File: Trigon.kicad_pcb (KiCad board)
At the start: 2 copper layers, 160 x 120 mm, 50 parts, among them U1 ProMicro

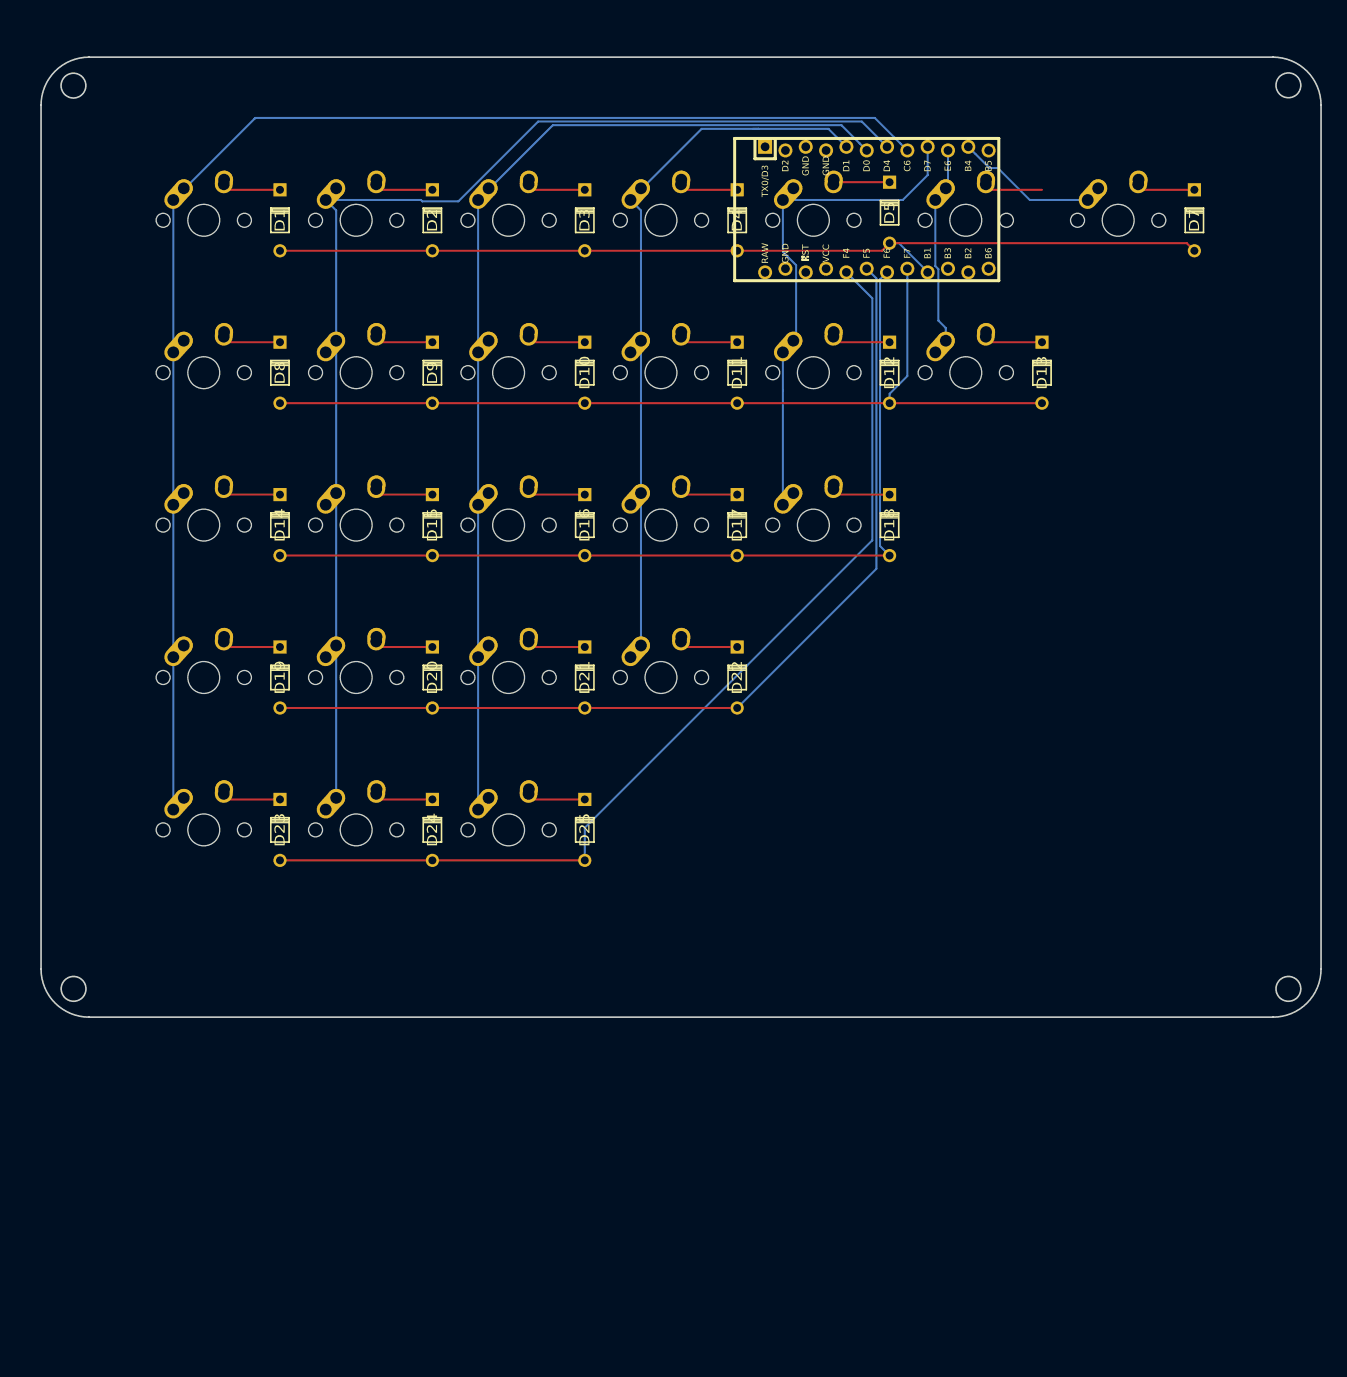
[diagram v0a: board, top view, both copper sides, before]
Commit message: routed without rows cols
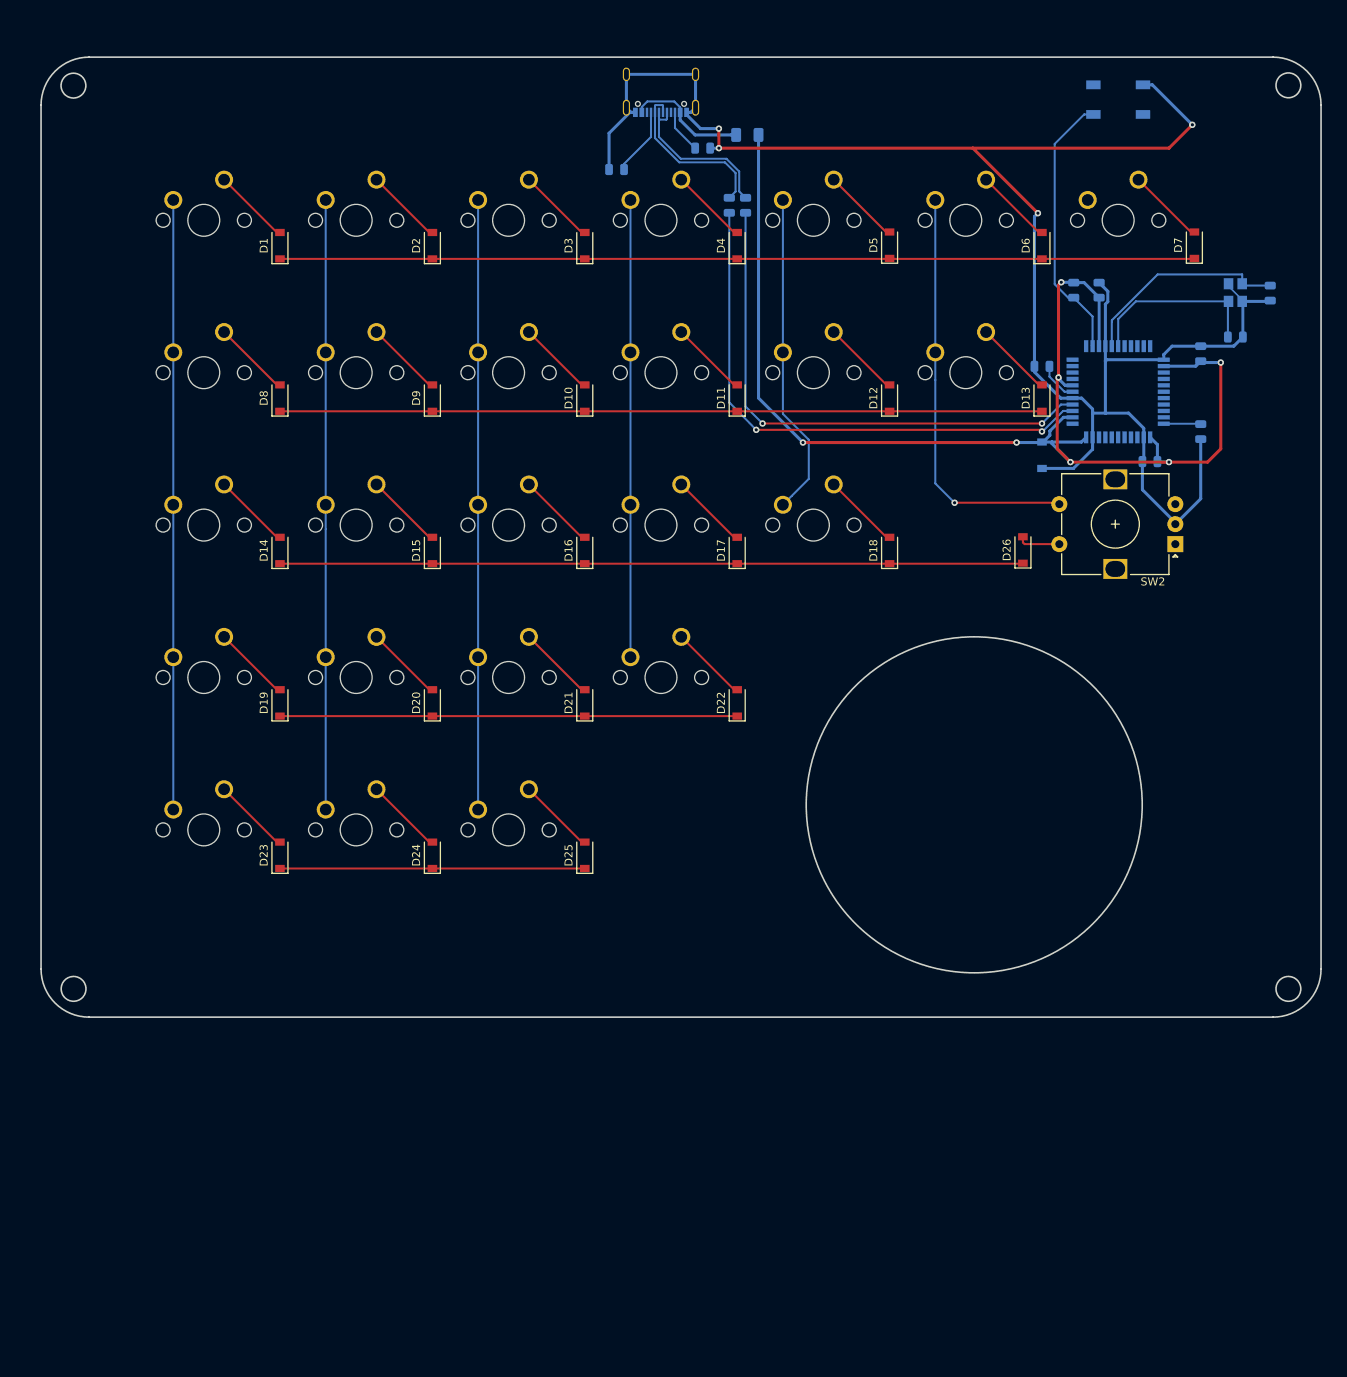
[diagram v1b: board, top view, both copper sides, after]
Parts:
- added C1: 22pF, Capacitor_SMD:C_0805_2012Metric, B.Cu at (148.0, -80.7)
- added C2: 22pF, Capacitor_SMD:C_0805_2012Metric, B.Cu at (152.4, -86.2)
- added C3: 1uF, Capacitor_SMD:C_0805_2012Metric, B.Cu at (123.8, -77.0)
- added C4: 0.1uF, Capacitor_SMD:C_0805_2012Metric, B.Cu at (143.7, -78.6)
- added C5: 0.1uF, Capacitor_SMD:C_0805_2012Metric, B.Cu at (137.3, -65.1)
- added C6: 0.1uF, Capacitor_SMD:C_0805_2012Metric, B.Cu at (131.0, -86.5)
- added C7: 10uF, Diode_SMD:D_SOD-123, B.Cu at (123.8, -65.9)
- added D26: D_Small, Diode_SMD:D_SOD-123, F.Cu at (121.4, -54.0)
- added D6: D_Small, Diode_SMD:D_SOD-123, F.Cu at (123.8, -92.1)
- added F1: Polyfuse_Small, Fuse:Fuse_1206_3216Metric, B.Cu at (87.0, -105.9)
- added J1: USB_C_Receptacle_USB2.0, Connector_USB:USB_C_Receptacle_Palconn_UTC16-G, B.Cu at (76.2, -111.3)
- added R1: 22, Resistor_SMD:R_0805_2012Metric, B.Cu at (86.8, -97.1)
- added R2: 22, Resistor_SMD:R_0805_2012Metric, B.Cu at (84.7, -97.1)
- added R3: 10k, Resistor_SMD:R_0805_2012Metric, B.Cu at (127.8, -86.5)
- added R4: R_Small, Resistor_SMD:R_0805_2012Metric, B.Cu at (70.6, -101.6)
- added R5: R_Small, Resistor_SMD:R_0805_2012Metric, B.Cu at (81.4, -104.3)
- added R6: 10k, Resistor_SMD:R_0805_2012Metric, B.Cu at (143.7, -68.8)
- added SW1: SW_Push, random-keyboard-parts:SKQG-1155865, B.Cu at (133.3, -110.3)
- added SW2: Rotary_Encoder_Switch, Rotary_Encoder:RotaryEncoder_Alps_EC12E-Switch_Vertical_H20mm, F.Cu at (140.5, -54.8)
- added Y1: 16MHz, Crystal:Crystal_SMD_3225-4Pin_3.2x2.5mm, B.Cu at (148.0, -86.2)
- D1, D10, D11, D12, D13, D14, D15, D16, D17, D18, D19, D2, D20, D21, D22, D23, D24, D25, D3, D4, D5, D7, D8, D9: footprint Keebio-Parts:Diode -> Diode_SMD:D_SOD-123
- MX1, MX10, MX11, MX12, MX13, MX14, MX15, MX16, MX17, MX18, MX19, MX2, MX20, MX21, MX22, MX23, MX24, MX25, MX3, MX4, MX5, MX6, MX7, MX8, MX9: footprint MX_Alps_Hybrid:MX-1U-NoLED -> MX_Only:MXOnly-1U-NoLED
- U1: value ProMicro -> ATmega32U4-AU; footprint Keebio-Parts:ArduinoProMicro-ZigZag -> Package_QFP:TQFP-44_10x10mm_P0.8mm
- moved U1 37.8 mm to (133.3, -73.8)
- moved D5 4.06 mm to (104.8, -92.1)
- moved D19 3.18 mm to (28.6, -34.9)
- moved D20 3.18 mm to (47.6, -34.9)
- moved D21 3.18 mm to (66.7, -34.9)
- moved D22 3.18 mm to (85.7, -34.9)
- moved D23 3.18 mm to (28.6, -15.9)
- moved D24 3.18 mm to (47.6, -15.9)
- moved D25 3.18 mm to (66.7, -15.9)
- moved D1 3.17 mm to (28.6, -92.1)
- moved D10 3.17 mm to (66.7, -73.0)
- moved D11 3.17 mm to (85.7, -73.0)
- moved D12 3.17 mm to (104.8, -73.0)
- moved D13 3.17 mm to (123.8, -73.0)
- moved D14 3.17 mm to (28.6, -54.0)
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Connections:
- U1 pad 10: COL5 -> Net-(U1-Pad10)
- U1 pad 11: COL6 -> Net-(U1-Pad11)
- U1 pad 14: Net-(U1-Pad14) -> +5V
- U1 pad 15: Net-(U1-Pad15) -> GND
- U1 pad 16: ROW0 -> Net-(C2-Pad1)
- U1 pad 17: ROW1 -> Net-(C1-Pad1)
- U1 pad 18: ROW2 -> Net-(U1-Pad18)
- U1 pad 19: ROW3 -> Net-(U1-Pad19)
- U1 pad 2: Net-(U1-Pad2) -> +5V
- U1 pad 20: ROW4 -> Net-(U1-Pad20)
- U1 pad 23: Net-(U1-Pad23) -> GND
- U1 pad 24: Net-(U1-Pad24) -> +5V
- U1 pad 5: COL3 -> GND
- U1 pad 6: COL2 -> Net-(C3-Pad1)
- U1 pad 7: COL1 -> +5V
- U1 pad 8: COL0 -> Net-(U1-Pad8)
- U1 pad 9: COL4 -> Net-(U1-Pad9)
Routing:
- net GND: track 0.00 -> 237.7 mm, vias 0 -> 4
- net +5V: track 0.00 -> 165.1 mm, vias 0 -> 7
- net COL0: track 174.0 -> 76.2 mm
- net ROW4: track 127.8 -> 38.1 mm
- net COL1: track 153.0 -> 76.2 mm
- net Net-(R2-Pad1): track 0.00 -> 70.0 mm, vias 0 -> 2
- net Net-(R1-Pad1): track 0.00 -> 66.9 mm, vias 0 -> 2
- net ROW3: track 119.8 -> 57.1 mm
- net COL2: track 130.0 -> 76.2 mm
- net COL3: track 92.5 -> 57.4 mm
- net Net-(R3-Pad2): track 0.00 -> 34.2 mm
- net COL5: track 25.0 -> 52.0 mm, vias 0 -> 1
- net Net-(C2-Pad1): track 0.00 -> 26.7 mm
- net Net-(C1-Pad1): track 0.00 -> 22.6 mm
- net COL4: track 62.4 -> 40.8 mm
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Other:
- outline, holes or cut-outs redrawn

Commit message: fully routed matrix
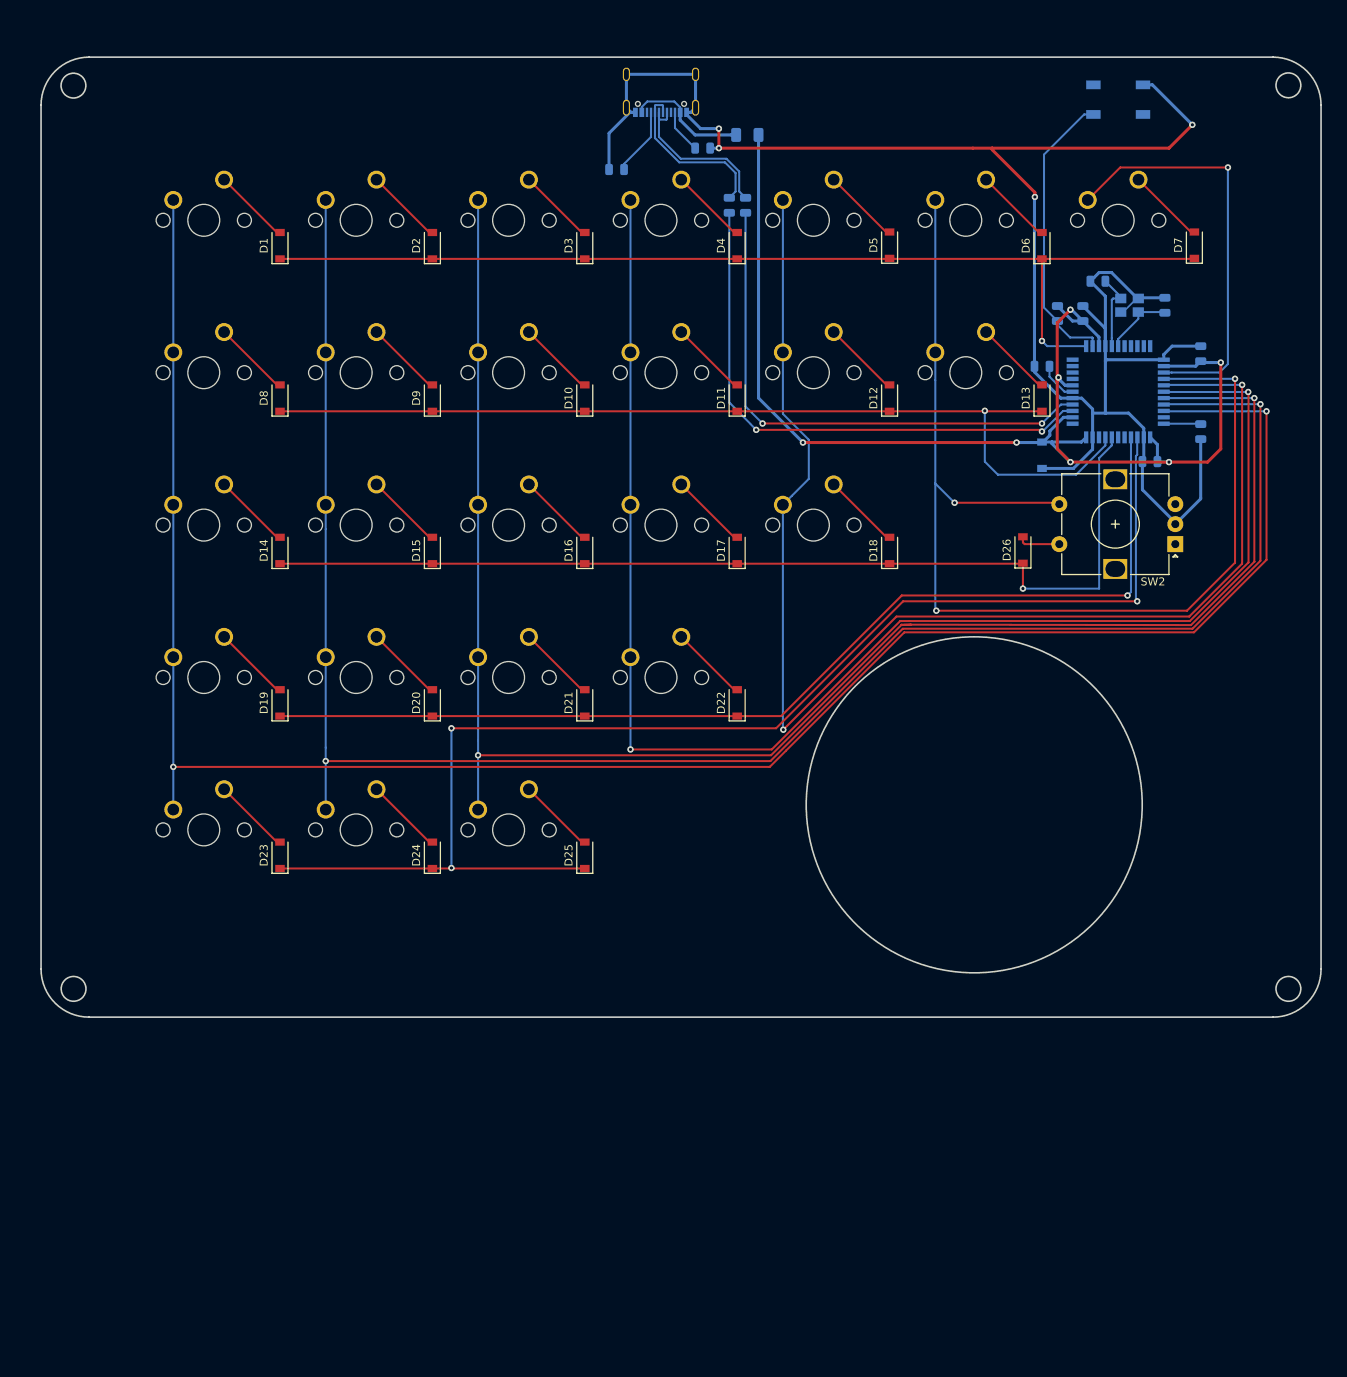
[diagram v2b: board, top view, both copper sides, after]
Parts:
- moved C2 21.6 mm to (130.8, -87.6), turned to 180 degrees
- moved Y1 13.3 mm to (134.8, -84.6), turned to 180 degrees
- moved C1 9.66 mm to (139.2, -84.6), turned to 90 degrees
- moved C6 3.56 mm to (128.9, -83.6)
- moved R3 3.56 mm to (125.8, -83.6)
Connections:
- U1 pad 12: Net-(U1-Pad12) -> ROW0
- U1 pad 25: Net-(U1-Pad25) -> COL6
- U1 pad 26: Net-(U1-Pad26) -> COL5
- U1 pad 27: Net-(U1-Pad27) -> COL4
- U1 pad 28: Net-(U1-Pad28) -> COL3
- U1 pad 29: Net-(U1-Pad29) -> COL2
- U1 pad 30: Net-(U1-Pad30) -> COL1
- U1 pad 31: Net-(U1-Pad31) -> COL0
- U1 pad 36: Net-(U1-Pad36) -> ROW4
- U1 pad 37: Net-(U1-Pad37) -> ROW3
- U1 pad 40: Net-(U1-Pad40) -> ROW2
- U1 pad 41: Net-(U1-Pad41) -> ROW1
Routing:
- net COL0: track 76.2 -> 255.0 mm, vias 0 -> 2
- net COL1: track 76.2 -> 235.4 mm, vias 0 -> 2
- net COL2: track 76.2 -> 216.5 mm, vias 0 -> 2
- net ROW4: track 38.1 -> 168.6 mm, vias 0 -> 3
- net COL3: track 57.4 -> 187.7 mm, vias 0 -> 2
- net COL4: track 40.8 -> 167.0 mm, vias 0 -> 2
- net COL5: track 52.0 -> 139.7 mm, vias 1 -> 3
- net ROW3: track 57.1 -> 132.1 mm, vias 0 -> 1
- net COL6: track 0.00 -> 52.2 mm, vias 0 -> 1
- net ROW2: track 92.9 -> 125.2 mm, vias 0 -> 1
- net ROW1: track 95.2 -> 120.0 mm, vias 0 -> 1
- net Net-(C2-Pad1): track 26.7 -> 10.2 mm
- net ROW0: track 114.3 -> 130.4 mm, vias 0 -> 1
- net Net-(C1-Pad1): track 22.6 -> 8.66 mm
- net +5V: track 165.1 -> 161.3 mm
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
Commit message: incorporate feedback
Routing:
- net GND: track 240.6 -> 239.6 mm
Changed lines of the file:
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@@
     (thickness 1.6)
     (drawings 13)
-    (tracks 411)
+    (tracks 413)
     (zones 0)
     (modules 70)
@@
   (segment (start 130.358027 -88.115527) (end 129.8725 -87.63) (width 0.381) (layer B.Cu) (net 41))
   (segment (start 135.866667 -85.476326) (end 135.766667 -85.476326) (width 0.381) (layer B.Cu) (net 41))
-  (segment (start 131.75 -85.7525) (end 131.75 -79.51875) (width 0.381) (layer B.Cu) (net 41))
   (segment (start 129.8725 -87.63) (end 131.75 -85.7525) (width 0.381) (layer B.Cu) (net 41))
   (segment (start 131.75 -81.722) (end 131.75 -79.51875) (width 0.381) (layer B.Cu) (net 41))
-  (segment (start 128.93675 -84.53525) (end 131.75 -81.722) (width 0.381) (layer B.Cu) (net 41))
+  (segment (start 131.36475 -84.53525) (end 131.7625 -84.1375) (width 0.381) (layer B.Cu) (net 41))
+  (segment (start 128.93675 -84.53525) (end 131.36475 -84.53525) (width 0.381) (layer B.Cu) (net 41))
+  (segment (start 131.7625 -84.1375) (end 131.75 -79.51875) (width 0.381) (layer B.Cu) (net 41))
+  (segment (start 131.75 -85.7525) (end 131.7625 -84.1375) (width 0.381) (layer B.Cu) (net 41))
   (segment (start 139.104501 -83.776326) (end 139.192 -83.688827) (width 0.254) (layer B.Cu) (net 42))
   (segment (start 135.866667 -83.776326) (end 139.104501 -83.776326) (width 0.254) (layer B.Cu) (net 42))
